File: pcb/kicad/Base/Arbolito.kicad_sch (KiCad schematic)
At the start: 56 parts, among them J1 Battery, J2 Conn_01x06_Female, P1 USB_C_Plug_USB2.0, Q1 S8050, Q2 S8050, Q3 S8050, SW1 SW_DP3T, SW2 SW_Push, SW3 SW_Push, SW4 SW_Push, U1 NCP115AMX120TCG, U2 CH340C, U3 AP63205WU, U4 ESP-12F, U5 SHTC1

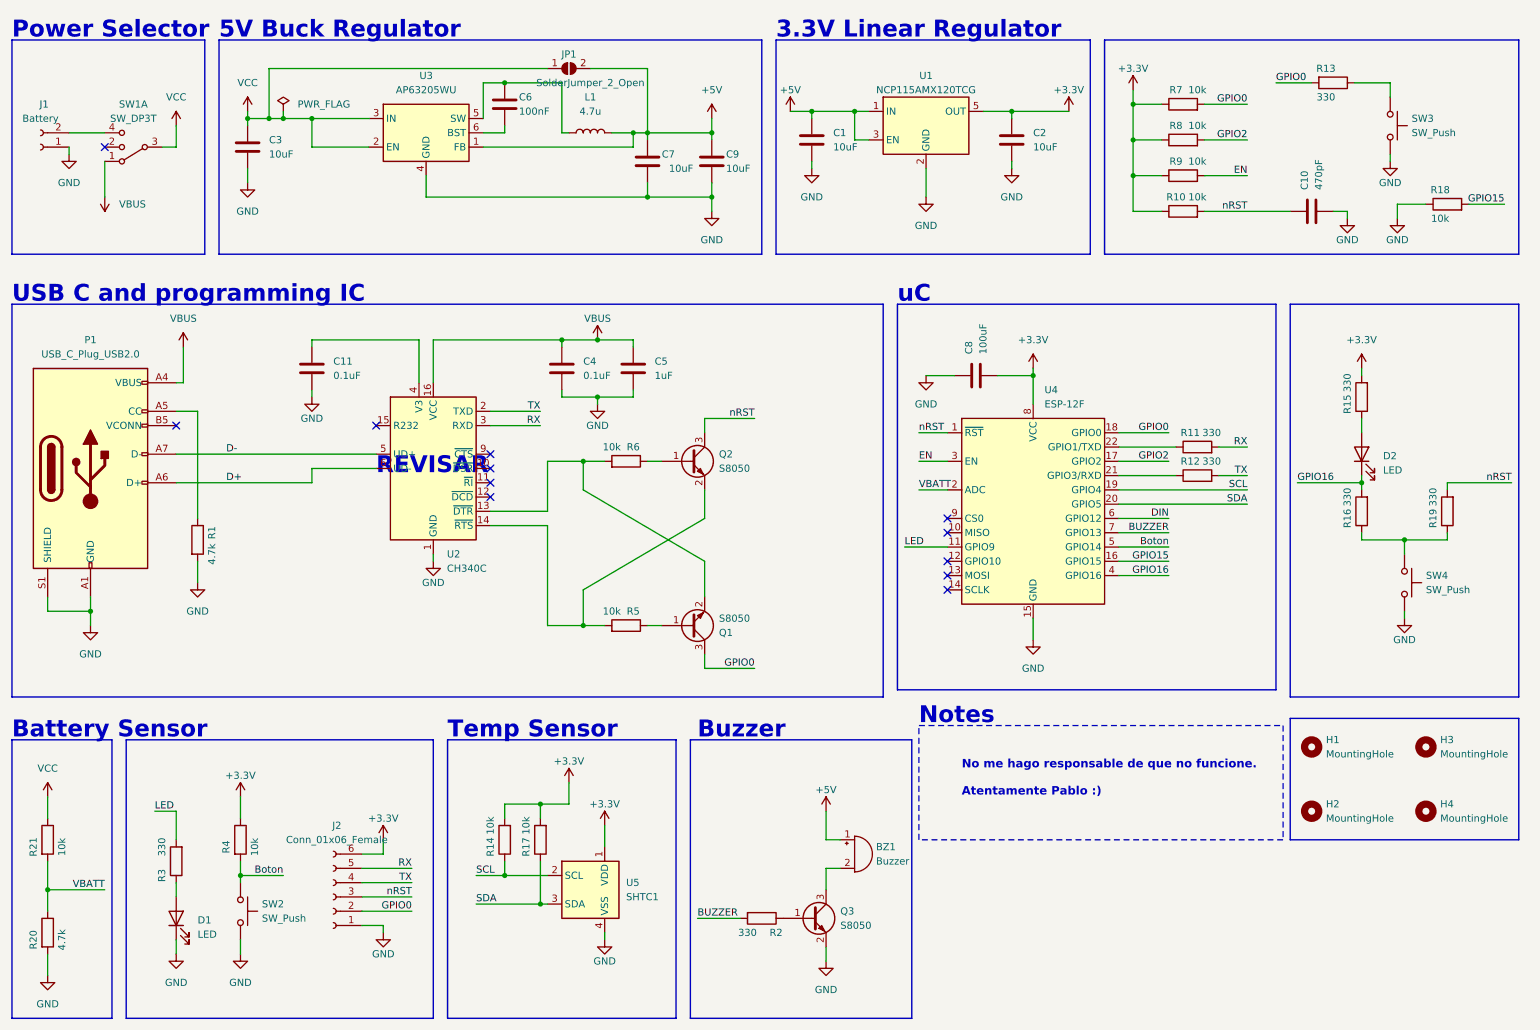
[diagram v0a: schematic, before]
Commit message: Switch and buttons
Switch and buttons changed on PCB
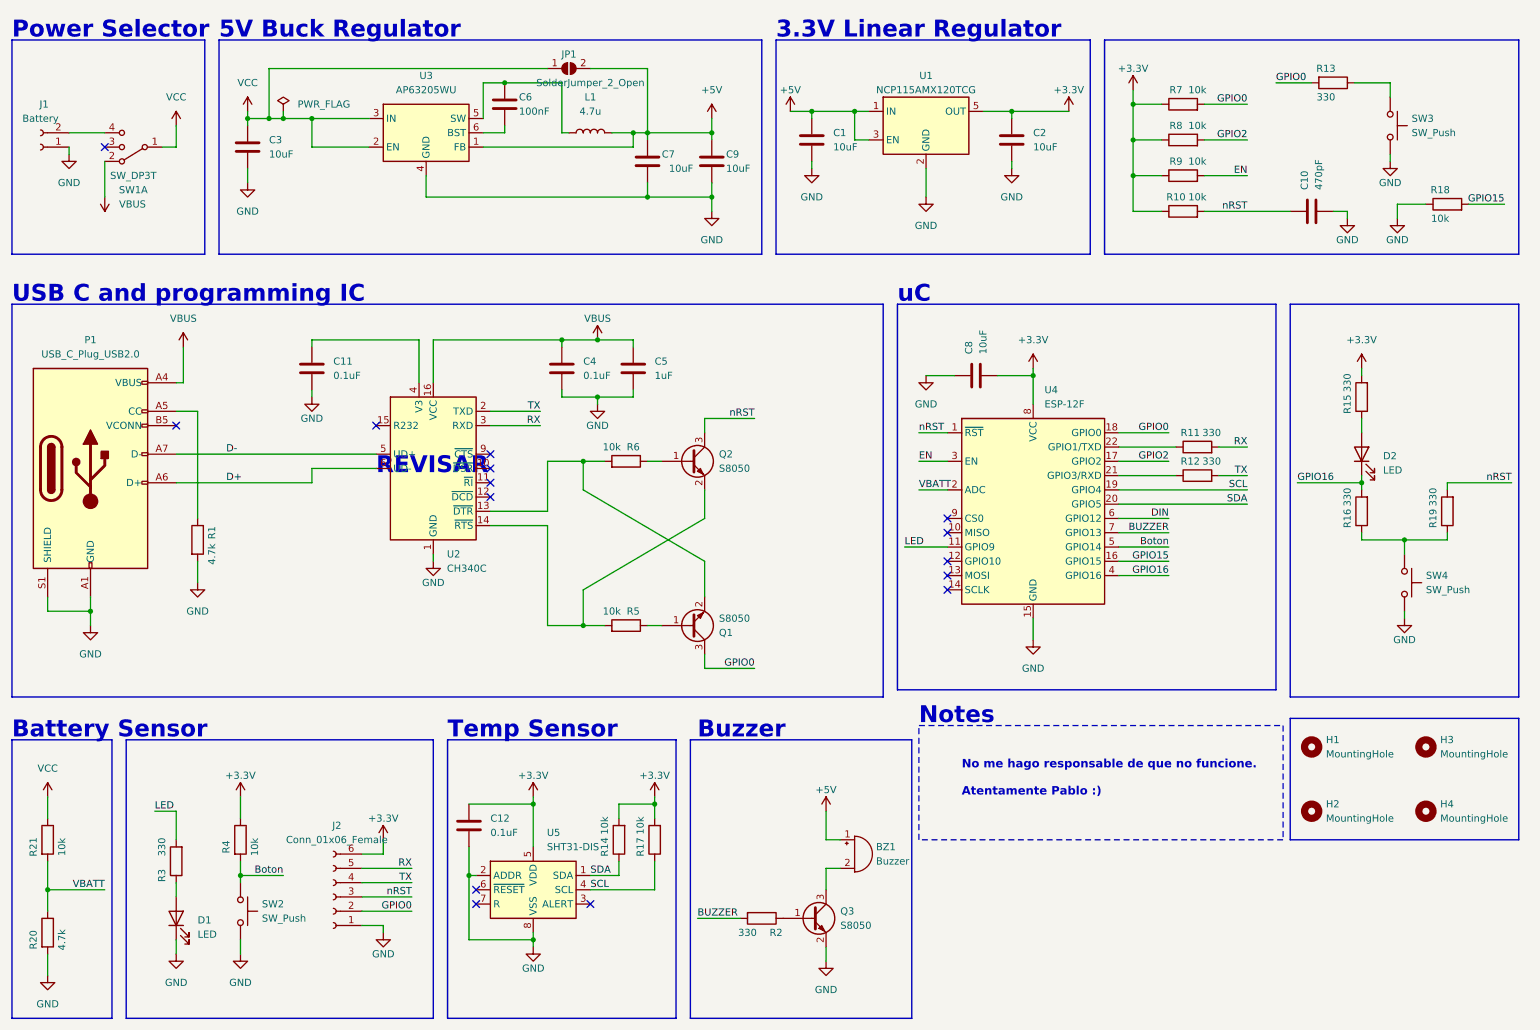
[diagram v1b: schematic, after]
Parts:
- removed U5: SHTC1, Sensor_Humidity:Sensirion_DFN-4-1EP_2x2mm_P1mm_EP0.7x1.6mm, symbol Sensor_Humidity:SHTC1
- added C12: 0.1uF, Capacitor_SMD:C_0805_2012Metric, symbol Device:C
- added U5: SHT31-DIS, Sensor_Humidity:Sensirion_DFN-8-1EP_2.5x2.5mm_P0.5mm_EP1.1x1.7mm, symbol Sensor_Humidity:SHT31-DIS
- C8: value 100uF -> 10uF
- SW1: footprint Library:3PSwitch -> Library:3PSwitch_Cheap
- SW2, SW3, SW4: footprint Button_Switch_SMD:SW_SPST_SKQG_WithoutStem -> Library:Button
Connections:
- net +3.3V: now also C12.1, U5.5 (VDD)
- net GND: now also C12.2, U5.2 (ADDR), U5.8 (VSS), U5.9 (VSS)
- net SCL: now also R17.1, U5.4 (SCL); no longer R14.1
- net SDA: now also R14.1, U5.1 (SDA); no longer R17.1
- net VBUS: now also SW1.2 (1); no longer SW1.1
- net VCC: now also SW1.1; no longer SW1.3
- no-connect marks 12 -> 15
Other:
- moved on the sheet: R14, R17

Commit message: Few leds version added
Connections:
- net GND: now also SW2.3 (2), SW3.3 (2), SW4.3 (2); no longer SW2.2, SW3.2, SW4.2
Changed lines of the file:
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@@
       (effects (font (size 1.27 1.27)) hide)
     )
+    (pin "1")
     (pin "2")
     (pin "3")
-    (pin "1")
     (pin "4")
     (pin "5")
@@
   (symbol (lib_id "Switch:SW_Push") (at 260.35 36.83 270) (unit 1)
     (in_bom yes) (on_board yes) (dnp no) (fields_autoplaced)
-    (property "Reference" "SW3" (at 264.16 35.5599 90)
-      (effects (font (size 1.27 1.27)) (justify left))
-    )
-    (property "Value" "SW_Push" (at 264.16 38.0999 90)
-      (effects (font (size 1.27 1.27)) (justify left))
-    )
-    (property "Footprint" "Library:Button" (at 265.43 36.83 0)
-      (effects (font (size 1.27 1.27)) hide)
-    )
-    (property "Datasheet" "~" (at 265.43 36.83 0)
-      (effects (font (size 1.27 1.27)) hide)
-    )
-    (pin "1")
-    (pin "2")
+    (property "Reference" "SW3" (at 261.6201 40.64 90)
+      (effects (font (size 1.27 1.27)) (justify left))
+    )
+    (property "Value" "SW_Push" (at 259.0801 40.64 90)
+      (effects (font (size 1.27 1.27)) (justify left))
+    )
+    (property "Footprint" "Library:Button" (at 260.35 41.91 0)
+      (effects (font (size 1.27 1.27)) hide)
+    )
+    (property "Datasheet" "~" (at 260.35 41.91 0)
+      (effects (font (size 1.27 1.27)) hide)
+    )
+    (pin "1")
+    (pin "3")
     (instances
       (project "Arbolito"
@@
     )
   )
-  (symbol (lib_id "Switch:SW_Push") (at 55.88 176.53 270) (unit 1)
-    (in_bom yes) (on_board yes) (dnp no) (fields_autoplaced)
-    (property "Reference" "SW2" (at 59.69 175.2599 90)
-      (effects (font (size 1.27 1.27)) (justify left))
-    )
-    (property "Value" "SW_Push" (at 59.69 177.7999 90)
-      (effects (font (size 1.27 1.27)) (justify left))
-    )
-    (property "Footprint" "Library:Button" (at 60.96 176.53 0)
-      (effects (font (size 1.27 1.27)) hide)
-    )
-    (property "Datasheet" "~" (at 60.96 176.53 0)
-      (effects (font (size 1.27 1.27)) hide)
-    )
-    (pin "1")
-    (pin "2")
+  (symbol (lib_name "SW_Push_2") (lib_id "Switch:SW_Push") (at 55.88 176.53 270) (unit 1)
+    (in_bom yes) (on_board yes) (dnp no) (fields_autoplaced)
+    (property "Reference" "SW2" (at 57.1501 180.34 90)
+      (effects (font (size 1.27 1.27)) (justify left))
+    )
+    (property "Value" "SW_Push" (at 54.6101 180.34 90)
+      (effects (font (size 1.27 1.27)) (justify left))
+    )
+    (property "Footprint" "Library:Button" (at 57.15 181.61 0)
+      (effects (font (size 1.27 1.27)) hide)
+    )
+    (property "Datasheet" "~" (at 55.88 181.61 0)
+      (effects (font (size 1.27 1.27)) hide)
+    )
+    (pin "1")
+    (pin "3")
     (instances
       (project "Arbolito"
@@
     )
   )
-  (symbol (lib_id "Switch:SW_Push") (at 262.89 118.11 270) (unit 1)
-    (in_bom yes) (on_board yes) (dnp no) (fields_autoplaced)
-    (property "Reference" "SW4" (at 266.7 116.8399 90)
-      (effects (font (size 1.27 1.27)) (justify left))
-    )
-    (property "Value" "SW_Push" (at 266.7 119.3799 90)
-      (effects (font (size 1.27 1.27)) (justify left))
-    )
-    (property "Footprint" "Library:Button" (at 267.97 118.11 0)
-      (effects (font (size 1.27 1.27)) hide)
-    )
-    (property "Datasheet" "~" (at 267.97 118.11 0)
-      (effects (font (size 1.27 1.27)) hide)
-    )
-    (pin "1")
-    (pin "2")
-    (instances
-      (project "Arbolito"
+  (symbol (lib_name "SW_Push_1") (lib_id "Switch:SW_Push") (at 262.89 118.11 270) (unit 1)
+    (in_bom yes) (on_board yes) (dnp no)
+    (property "Reference" "SW4" (at 266.7 119.38 90)
+      (effects (font (size 1.27 1.27)) (justify left))
+    )
+    (property "Value" "SW_Push" (at 266.7 116.84 90)
+      (effects (font (size 1.27 1.27)) (justify left))
+    )
+    (property "Footprint" "Library:Button" (at 262.89 124.46 0)
+      (effects (font (size 1.27 1.27)) hide)
+    )
+    (property "Datasheet" "~" (at 262.89 123.19 0)
+      (effects (font (size 1.27 1.27)) hide)
+    )
+    (pin "1")
+    (pin "3")
+    (instances
+      (project "Arbolito"

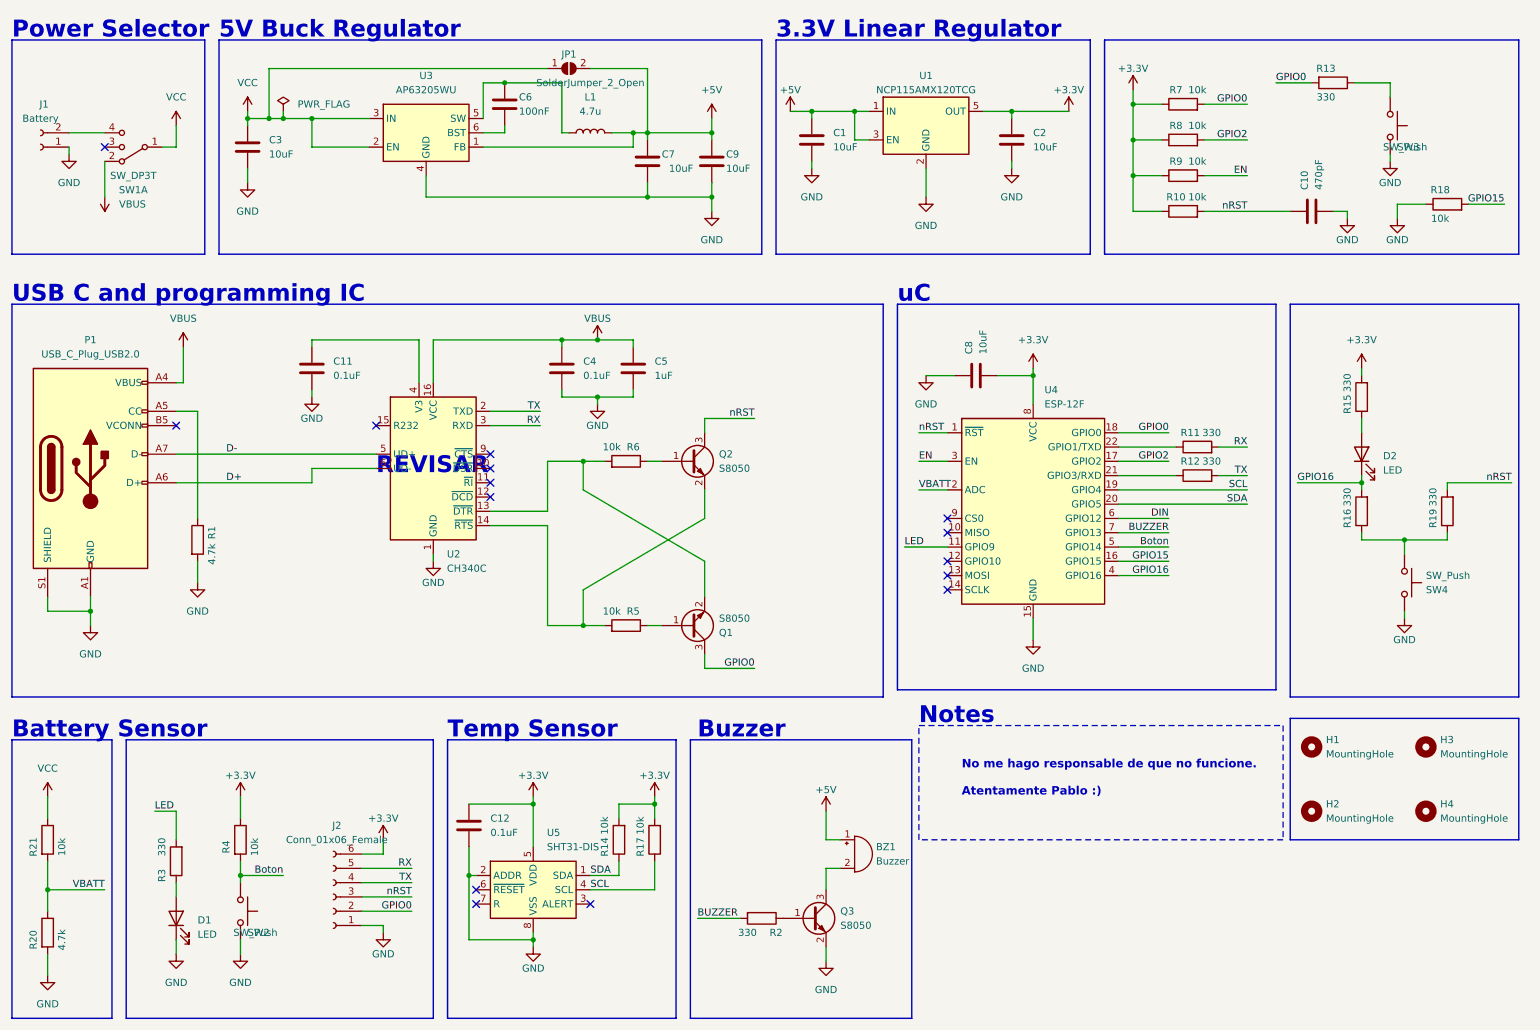
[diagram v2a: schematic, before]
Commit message: Footprints corrected
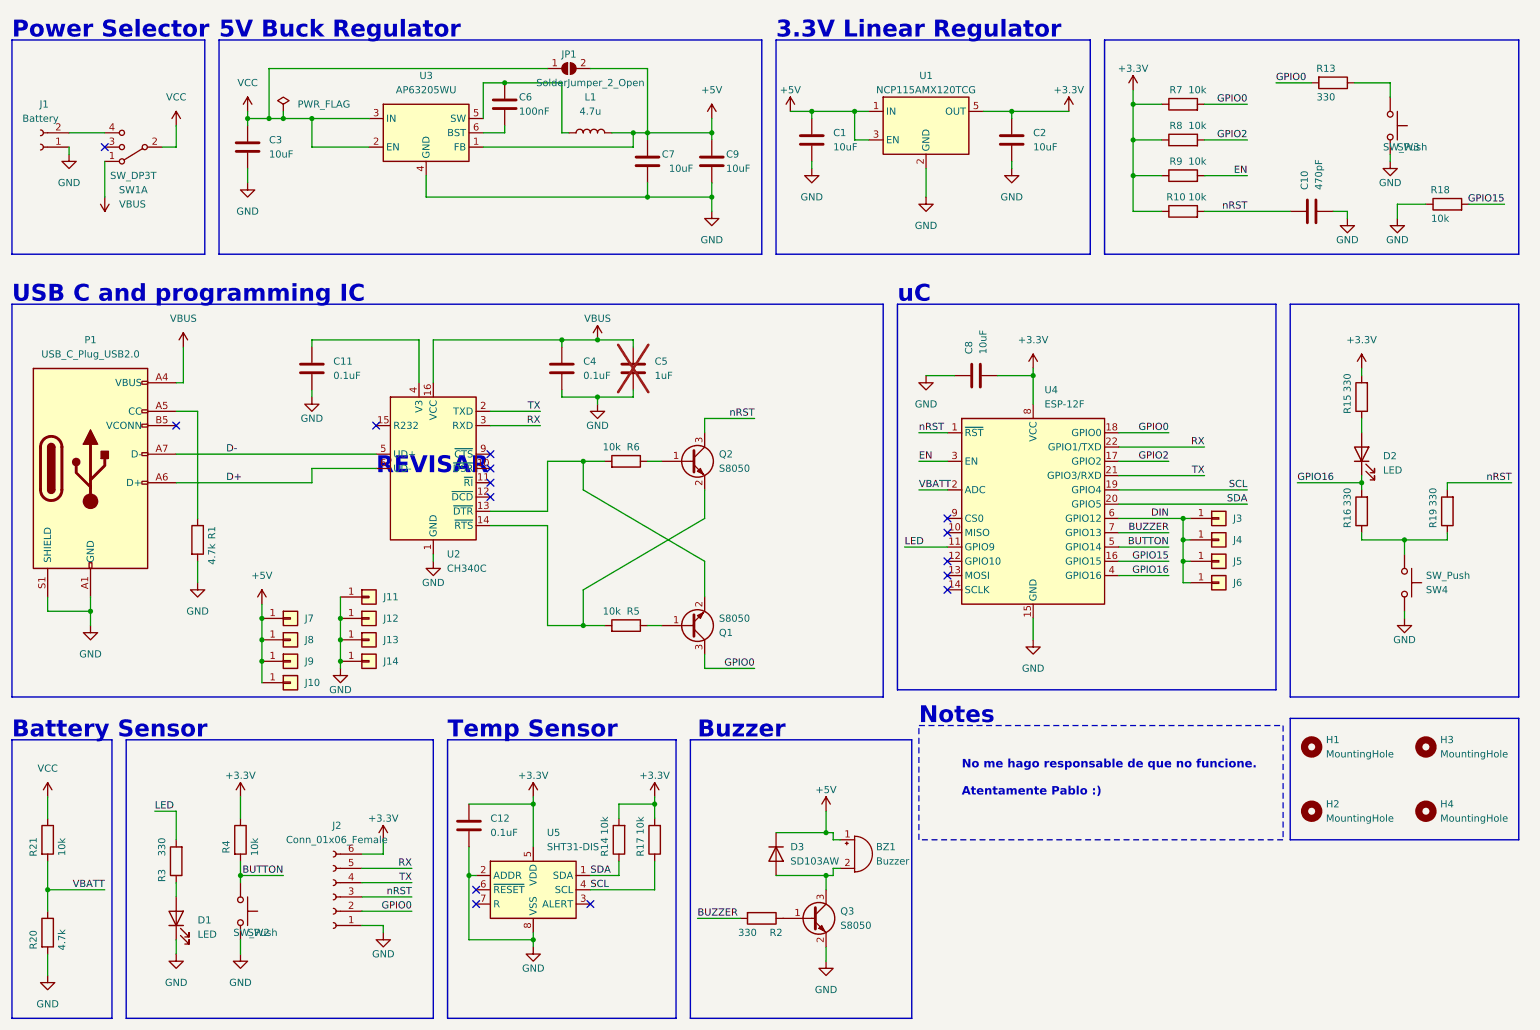
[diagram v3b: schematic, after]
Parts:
- removed R11, R12: 330, Resistor_SMD:R_0805_2012Metric_Pad1.20x1.40mm_HandSolder, symbol Device:R
- added D3: SD103AW, Diode_SMD:D_SOD-123, symbol Diode:1N5400
- added J10, J11, J12, J13, J14, J7, J8, J9: Conn_01x01, Library:Pad_tree_PS, symbol Connector_Generic:Conn_01x01
- added J3, J4, J5, J6: Conn_01x01, Library:Pad_tree_Data, symbol Connector_Generic:Conn_01x01
- C5: now not fitted
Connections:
- net +5V: now also D3.1 (K), J10.1 (Pin_1), J7.1 (Pin_1), J8.1 (Pin_1), J9.1 (Pin_1)
- net DIN: now also J3.1 (Pin_1), J4.1 (Pin_1), J5.1 (Pin_1), J6.1 (Pin_1)
- net GND: now also J11.1 (Pin_1), J12.1 (Pin_1), J13.1 (Pin_1), J14.1 (Pin_1)
- net RX: now also U4.22 (GPIO1/TXD)
- net TX: now also U4.21 (GPIO3/RXD)
- net VBUS: now also SW1.1; no longer SW1.2 (1)
- net VCC: now also SW1.2 (1); no longer SW1.1
- net at BZ1.2 (+), Q3.3 (C): now also D3.2 (A)
- net Boton renamed BUTTON
